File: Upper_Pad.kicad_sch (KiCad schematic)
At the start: 66 parts, among them SW13 DIR, SW14 F-PLN, SW15 AIR PORT, SW16 →, SW17 PROG, SW18 RAD NAV, SW20 ↓, SW21 BRT, SW22 DIM, SW25 PERF, SW26 FUEL PRED, SW29 INIT, SW30 SEC F-PLN, SW31 A, SW32 K, SW33 DATA, SW34 ATC COMM, SW35 B, SW36 L, SW38 MCDU MENU, SW39 C, SW40 M, SW41 ←, SW42 ↑, SW44 F, SW45 G, SW46 H, SW50 D, SW51 I, SW52 N, SW55 E, SW56 J, SW57 O

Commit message: Finished all button
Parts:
- added D19, D23, D24, D27, D28, D37, D43, D47, D48, D49, D53, D54: 1N4148, Diode_THT:D_DO-35_SOD27_P7.62mm_Horizontal, symbol Diode:1N4148
- added SW19: LSK1L, 1825910_6:SW_1825910-6-4, symbol 1825910-6:1825910-6
- added SW23: LSK2L, 1825910_6:SW_1825910-6-4, symbol 1825910-6:1825910-6
- added SW24: LSK3L, 1825910_6:SW_1825910-6-4, symbol 1825910-6:1825910-6
- added SW27: LSK4L, 1825910_6:SW_1825910-6-4, symbol 1825910-6:1825910-6
- added SW28: LSK5L, 1825910_6:SW_1825910-6-4, symbol 1825910-6:1825910-6
- added SW37: LSK6L, 1825910_6:SW_1825910-6-4, symbol 1825910-6:1825910-6
- added SW43: LSK1R, 1825910_6:SW_1825910-6-4, symbol 1825910-6:1825910-6
- added SW47: LSK2R, 1825910_6:SW_1825910-6-4, symbol 1825910-6:1825910-6
- added SW48: LSK3R, 1825910_6:SW_1825910-6-4, symbol 1825910-6:1825910-6
- added SW49: LSK4R, 1825910_6:SW_1825910-6-4, symbol 1825910-6:1825910-6
- added SW53: LSK5R, 1825910_6:SW_1825910-6-4, symbol 1825910-6:1825910-6
- added SW54: LSK6R, 1825910_6:SW_1825910-6-4, symbol 1825910-6:1825910-6
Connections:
- net COL_1: now also SW19.1
- net COL_2: now also SW23.1, SW24.1, SW27.1
- net COL_5: now also SW28.1
- net COL_6: now also SW37.1, SW43.1
- net COL_7: now also SW47.1, SW48.1
- net COL_8: now also SW49.1, SW53.1, SW54.1
- net ROW_0: now also D28.1 (K), D37.1 (K), D48.1 (K)
- net ROW_1: now also D43.1 (K), D47.1 (K)
- net ROW_2: now also D19.1 (K), D23.1 (K)
- net ROW_3: now also D24.1 (K)
- net ROW_4: now also D27.1 (K)
- new net: D23.2 (A), SW23.3
- new net: D28.2 (A), SW28.3
- new net: D24.2 (A), SW24.3
- new net: D49.2 (A), SW49.3
- new net: D27.2 (A), SW27.3
- new net: D48.2 (A), SW48.3
- new net: D53.2 (A), SW53.3
- new net: D54.2 (A), SW54.3
- new net: D47.2 (A), SW47.3
- new net: D19.2 (A), SW19.3
- new net: D43.2 (A), SW43.3
- new net: D37.2 (A), SW37.3
- no-connect marks 66 -> 90

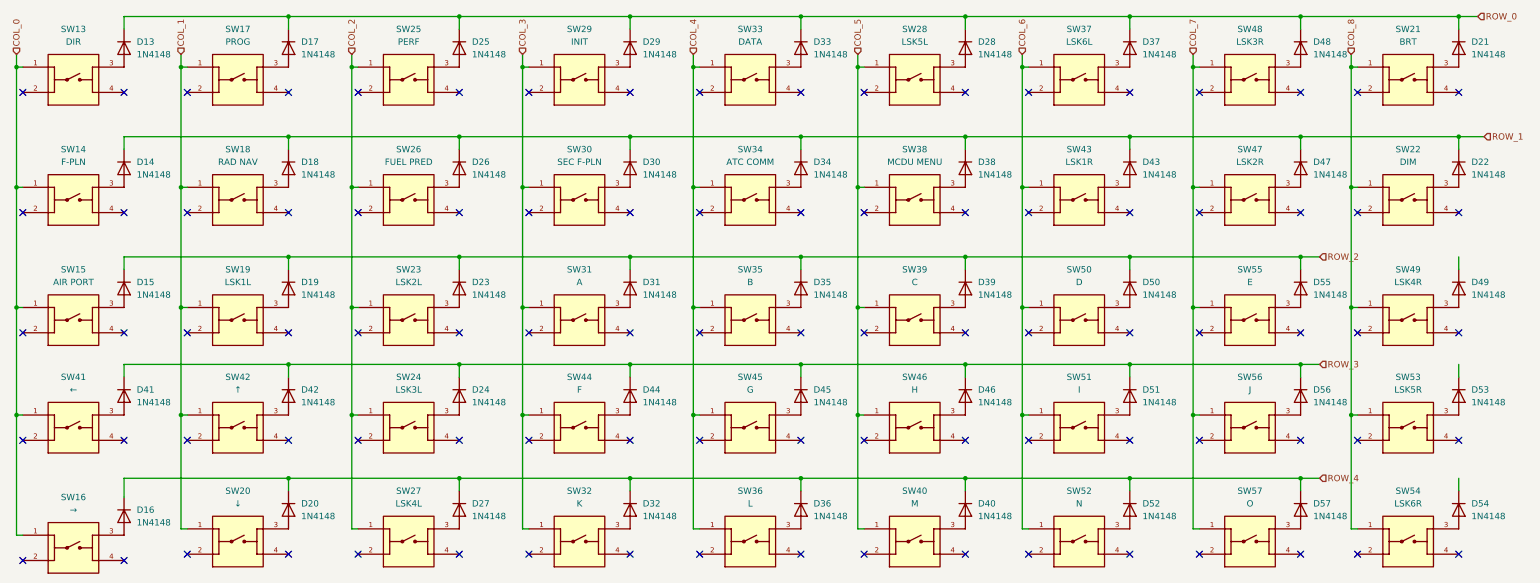
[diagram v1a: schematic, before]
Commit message: Add: PCB Part, NumPad Mesurement
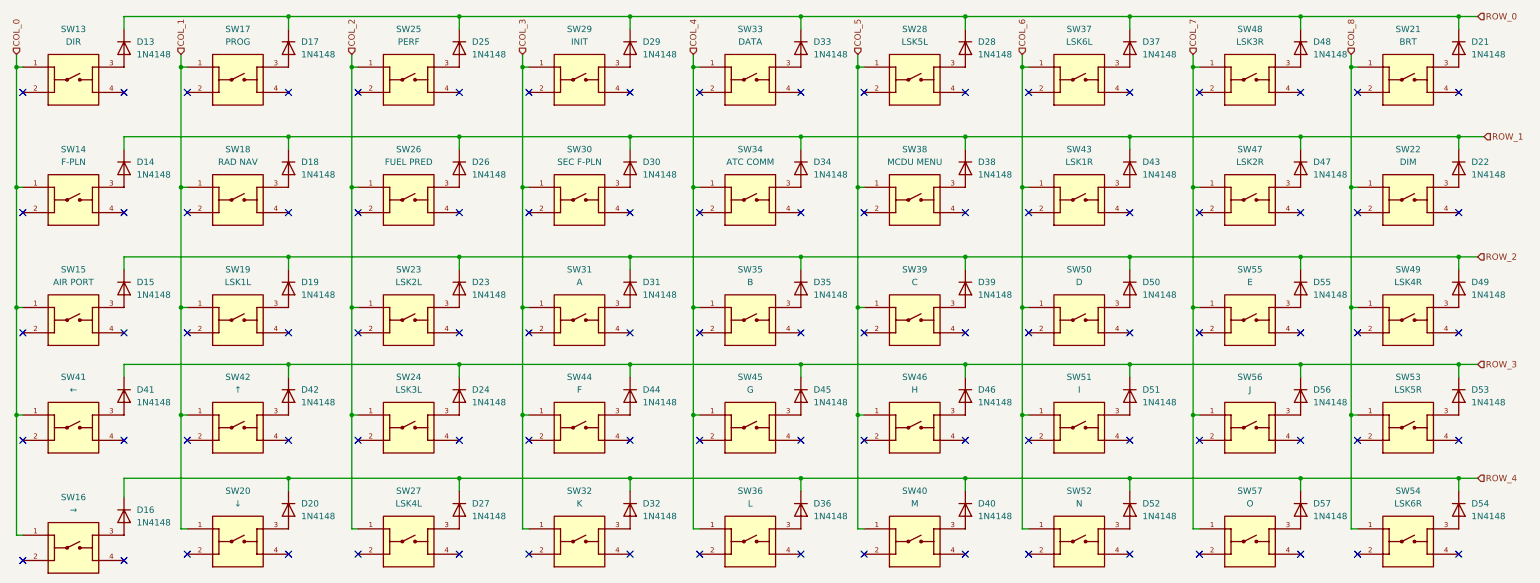
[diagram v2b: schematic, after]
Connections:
- net ROW_2: now also D49.1 (K)
- net ROW_3: now also D53.1 (K)
- net ROW_4: now also D54.1 (K)
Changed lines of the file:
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@@
+	)
+	(junction
+		(at 304.8 88.9)
+		(diameter 0)
+		(color 0 0 0 0)
 	)
 	(junction
@@
 	)
 	(junction
+		(at 304.8 67.31)
+		(diameter 0)
+		(color 0 0 0 0)
+	)
+	(junction
 		(at 238.76 19.05)
 		(diameter 0)
@@
 	)
 	(junction
+		(at 273.05 19.05)
+		(diameter 0)
+		(color 0 0 0 0)
+	)
+	(junction
+		(at 238.76 67.31)
+		(diameter 0)
+		(color 0 0 0 0)
+	)
+	(junction
+		(at 116.84 99.06)
+		(diameter 0)
+		(color 0 0 0 0)
+	)
+	(junction
+		(at 205.74 19.05)
+		(diameter 0)
+		(color 0 0 0 0)
+	)
+	(junction
+		(at 104.14 19.05)
+		(diameter 0)
+		(color 0 0 0 0)
+	)
+	(junction
+		(at 217.17 99.06)
+		(diameter 0)
+		(color 0 0 0 0)
+	)
+	(junction
+		(at 104.14 67.31)
+		(diameter 0)
+		(color 0 0 0 0)
+	)
+	(junction
+		(at 172.72 88.9)
+		(diameter 0)
+		(color 0 0 0 0)
+	)
+	(junction
+		(at 184.15 29.21)
+		(diameter 0)
+		(color 0 0 0 0)
+	)
+	(junction
+		(at 151.13 29.21)
+		(diameter 0)
+		(color 0 0 0 0)
+	)
+	(junction
+		(at 15.24 77.47)
+		(diameter 0)
+		(color 0 0 0 0)
+	)
+	(junction
+		(at 15.24 29.21)
+		(diameter 0)
+		(color 0 0 0 0)
+	)
+	(junction
+		(at 273.05 111.76)
+		(diameter 0)
+		(color 0 0 0 0)
+	)
+	(junction
 		(at 69.85 88.9)
 		(diameter 0)
@@
 	)
 	(junction
-		(at 273.05 19.05)
-		(diameter 0)
-		(color 0 0 0 0)
-	)
-	(junction
-		(at 238.76 67.31)
-		(diameter 0)
-		(color 0 0 0 0)
-	)
-	(junction
-		(at 116.84 99.06)
-		(diameter 0)
-		(color 0 0 0 0)
-	)
-	(junction
-		(at 205.74 19.05)
-		(diameter 0)
-		(color 0 0 0 0)
-	)
-	(junction
-		(at 104.14 19.05)
-		(diameter 0)
-		(color 0 0 0 0)
-	)
-	(junction
-		(at 217.17 99.06)
-		(diameter 0)
-		(color 0 0 0 0)
-	)
-	(junction
-		(at 104.14 67.31)
-		(diameter 0)
-		(color 0 0 0 0)
-	)
-	(junction
-		(at 172.72 88.9)
-		(diameter 0)
-		(color 0 0 0 0)
-	)
-	(junction
-		(at 184.15 29.21)
-		(diameter 0)
-		(color 0 0 0 0)
-	)
-	(junction
-		(at 151.13 29.21)
-		(diameter 0)
-		(color 0 0 0 0)
-	)
-	(junction
-		(at 15.24 77.47)
-		(diameter 0)
-		(color 0 0 0 0)
-	)
-	(junction
-		(at 15.24 29.21)
-		(diameter 0)
-		(color 0 0 0 0)
-	)
-	(junction
-		(at 273.05 111.76)
-		(diameter 0)
-		(color 0 0 0 0)
-	)
-	(junction
 		(at 48.26 29.21)
 		(diameter 0)
@@
 	)
 	(junction
+		(at 273.05 67.31)
+		(diameter 0)
+		(color 0 0 0 0)
+	)
+	(junction
+		(at 82.55 99.06)
+		(diameter 0)
+		(color 0 0 0 0)
+	)
+	(junction
+		(at 116.84 53.34)
+		(diameter 0)
+		(color 0 0 0 0)
+	)
+	(junction
+		(at 116.84 77.47)
+		(diameter 0)
+		(color 0 0 0 0)
+	)
+	(junction
+		(at 138.43 19.05)
+		(diameter 0)
+		(color 0 0 0 0)
+	)
+	(junction
+		(at 151.13 77.47)
+		(diameter 0)
+		(color 0 0 0 0)
+	)
+	(junction
+		(at 69.85 19.05)
+		(diameter 0)
+		(color 0 0 0 0)
+	)
+	(junction
 		(at 69.85 111.76)
 		(diameter 0)
@@
 	)
 	(junction
-		(at 273.05 67.31)
-		(diameter 0)
-		(color 0 0 0 0)
-	)
-	(junction
-		(at 82.55 99.06)
-		(diameter 0)
-		(color 0 0 0 0)
-	)
-	(junction
-		(at 116.84 53.34)
-		(diameter 0)
-		(color 0 0 0 0)
-	)
-	(junction
-		(at 116.84 77.47)
-		(diameter 0)
-		(color 0 0 0 0)
-	)
-	(junction
-		(at 138.43 19.05)
-		(diameter 0)
-		(color 0 0 0 0)
-	)
-	(junction
-		(at 151.13 77.47)
-		(diameter 0)
-		(color 0 0 0 0)
-	)
-	(junction
-		(at 69.85 19.05)
-		(diameter 0)
-		(color 0 0 0 0)
-	)
-	(junction
 		(at 304.8 19.05)
 		(diameter 0)
@@
 	)
 	(junction
+		(at 304.8 111.76)
+		(diameter 0)
+		(color 0 0 0 0)
+	)
+	(junction
 		(at 304.8 43.18)
 		(diameter 0)
@@
 	(wire
 		(pts
+			(xy 304.8 67.31) (xy 308.61 67.31)
+		)
+		(stroke
+			(width 0)
+			(type default)
+		)
+	)
+	(wire
+		(pts
 			(xy 172.72 19.05) (xy 172.72 21.59)
 		)
@@
 	(wire
 		(pts
-			(xy 69.85 88.9) (xy 276.86 88.9)
+			(xy 69.85 88.9) (xy 304.8 88.9)
 		)
 		(stroke
@@
 	(wire
 		(pts
-			(xy 36.83 67.31) (xy 276.86 67.31)
+			(xy 36.83 67.31) (xy 304.8 67.31)
 		)
 		(stroke
@@
 	(wire
 		(pts
-			(xy 69.85 111.76) (xy 276.86 111.76)
+			(xy 69.85 111.76) (xy 304.8 111.76)
 		)
 		(stroke
@@
 	(wire
 		(pts
+			(xy 304.8 88.9) (xy 308.61 88.9)
+		)
+		(stroke
+			(width 0)
+			(type default)
+		)
+	)
+	(wire
+		(pts
 			(xy 238.76 19.05) (xy 238.76 21.59)
 		)
@@
 	(wire
 		(pts
+			(xy 251.46 99.06) (xy 252.73 99.06)
+		)
+		(stroke
+			(width 0)
+			(type default)
+		)
+	)
+	(wire
+		(pts
+			(xy 116.84 77.47) (xy 116.84 99.06)
+		)
+		(stroke
+			(width 0)
+			(type default)
+		)
+	)
+	(wire
+		(pts
+			(xy 251.46 121.92) (xy 252.73 121.92)
+		)
+		(stroke
+			(width 0)
+			(type default)
+		)
+	)
+	(wire
+		(pts
+			(xy 217.17 29.21) (xy 218.44 29.21)
+		)
+		(stroke
+			(width 0)
+			(type default)
+		)
+	)
+	(wire
+		(pts
+			(xy 151.13 77.47) (xy 152.4 77.47)
+		)
+		(stroke
+			(width 0)
+			(type default)
+		)
+	)
+	(wire
+		(pts
+			(xy 15.24 53.34) (xy 16.51 53.34)
+		)
+		(stroke
+			(width 0)
+			(type default)
+		)
+	)
+	(wire
+		(pts
 			(xy 304.8 111.76) (xy 304.8 114.3)
 		)
@@
 	(wire
 		(pts
-			(xy 251.46 99.06) (xy 252.73 99.06)
-		)
-		(stroke
-			(width 0)
-			(type default)
-		)
-	)
-	(wire
-		(pts
-			(xy 116.84 77.47) (xy 116.84 99.06)
-		)
-		(stroke
-			(width 0)
-			(type default)
-		)
-	)
-	(wire
-		(pts
-			(xy 251.46 121.92) (xy 252.73 121.92)
-		)
-		(stroke
-			(width 0)
-			(type default)
-		)
-	)
-	(wire
-		(pts
-			(xy 217.17 29.21) (xy 218.44 29.21)
-		)
-		(stroke
-			(width 0)
-			(type default)
-		)
-	)
-	(wire
-		(pts
-			(xy 151.13 77.47) (xy 152.4 77.47)
-		)
-		(stroke
-			(width 0)
-			(type default)
-		)
-	)
-	(wire
-		(pts
-			(xy 15.24 53.34) (xy 16.51 53.34)
-		)
-		(stroke
-			(width 0)
-			(type default)
-		)
-	)
-	(wire
-		(pts
 			(xy 238.76 43.18) (xy 238.76 45.72)
+		)
+		(stroke
+			(width 0)
+			(type default)
+		)
+	)
+	(wire
+		(pts
+			(xy 304.8 111.76) (xy 308.61 111.76)
 		)
 		(stroke
@@
 	(hierarchical_label "ROW_4"
 		(shape input)
-		(at 276.86 111.76 0)
+		(at 308.61 111.76 0)
 		(effects
 			(font
@@
 	(hierarchical_label "ROW_3"
 		(shape input)
-		(at 276.86 88.9 0)
+		(at 308.61 88.9 0)
 		(effects
 			(font
@@
 	(hierarchical_label "ROW_2"
 		(shape input)
-		(at 276.86 67.31 0)
+		(at 308.61 67.31 0)
 		(effects
 			(font
